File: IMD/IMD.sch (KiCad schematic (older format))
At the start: 6 parts

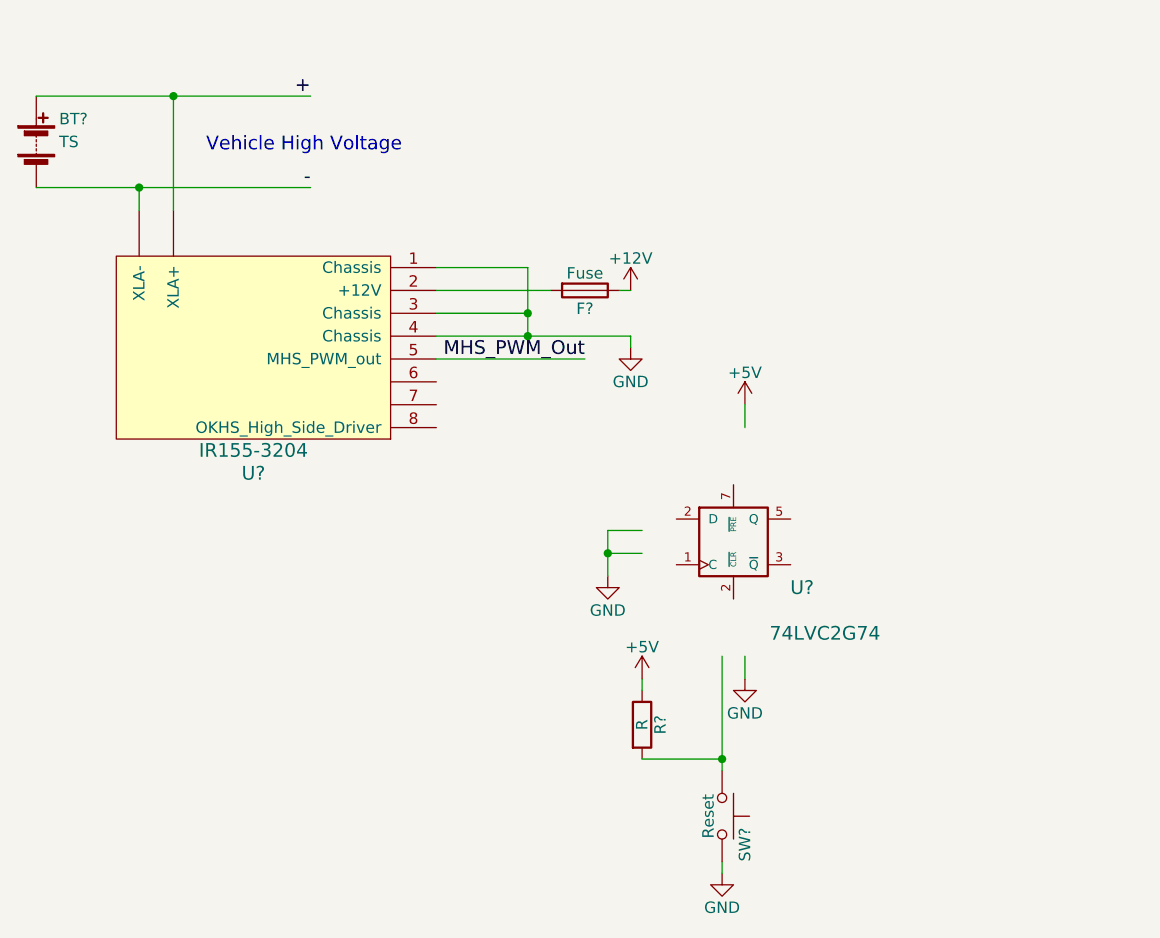
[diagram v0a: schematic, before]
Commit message: BSPD is more fleshed out. IMD latching continuing
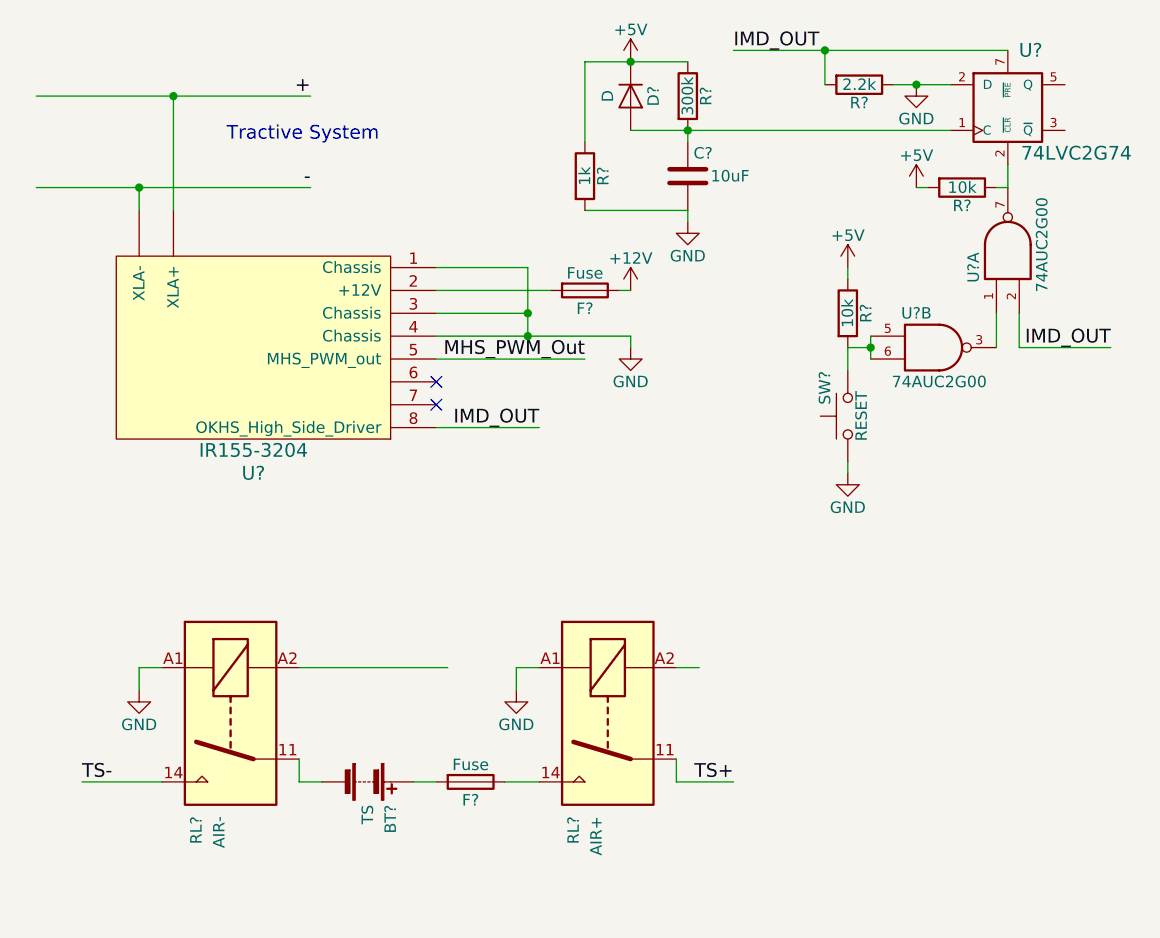
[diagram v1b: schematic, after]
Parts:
- removed R?: R, symbol R
- removed SW?: Reset, symbol SW_Push
- added C?: 10uF, symbol C
- added D?: D, symbol D
- added F?: Fuse, symbol Fuse
- added R?: 2.2k, symbol R
- added R?: 300k, symbol R
- added R?: 1k, symbol R
- added R? (x2): 10k, symbol R
- added RL?: AIR-, symbol Relay-SPST
- added RL?: AIR+, symbol Relay-SPST
- added SW?: RESET, symbol SW_Push
- added U? (x2): 74AUC2G00, symbol 74AUC2G00
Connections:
- net labels added: IMD_OUT, TS+, TS-
- wire segments 21 -> 46
- no-connect marks 0 -> 2
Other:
- note added: "Tractive System\n\n"
- note removed: "Vehicle High Voltage\n"
- moved on the sheet: BT?, U?

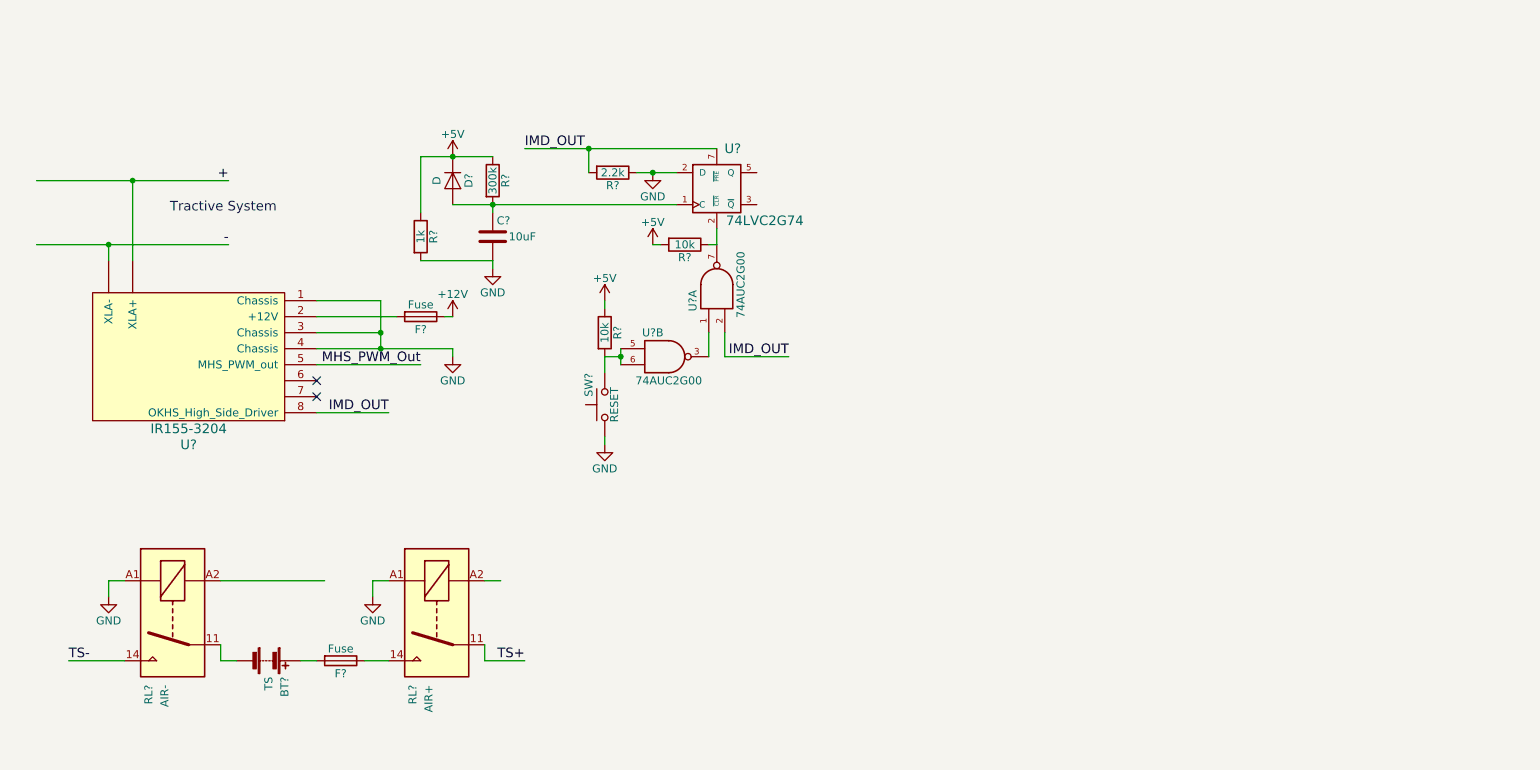
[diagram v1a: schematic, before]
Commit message: ESF-related changes to current system schematics
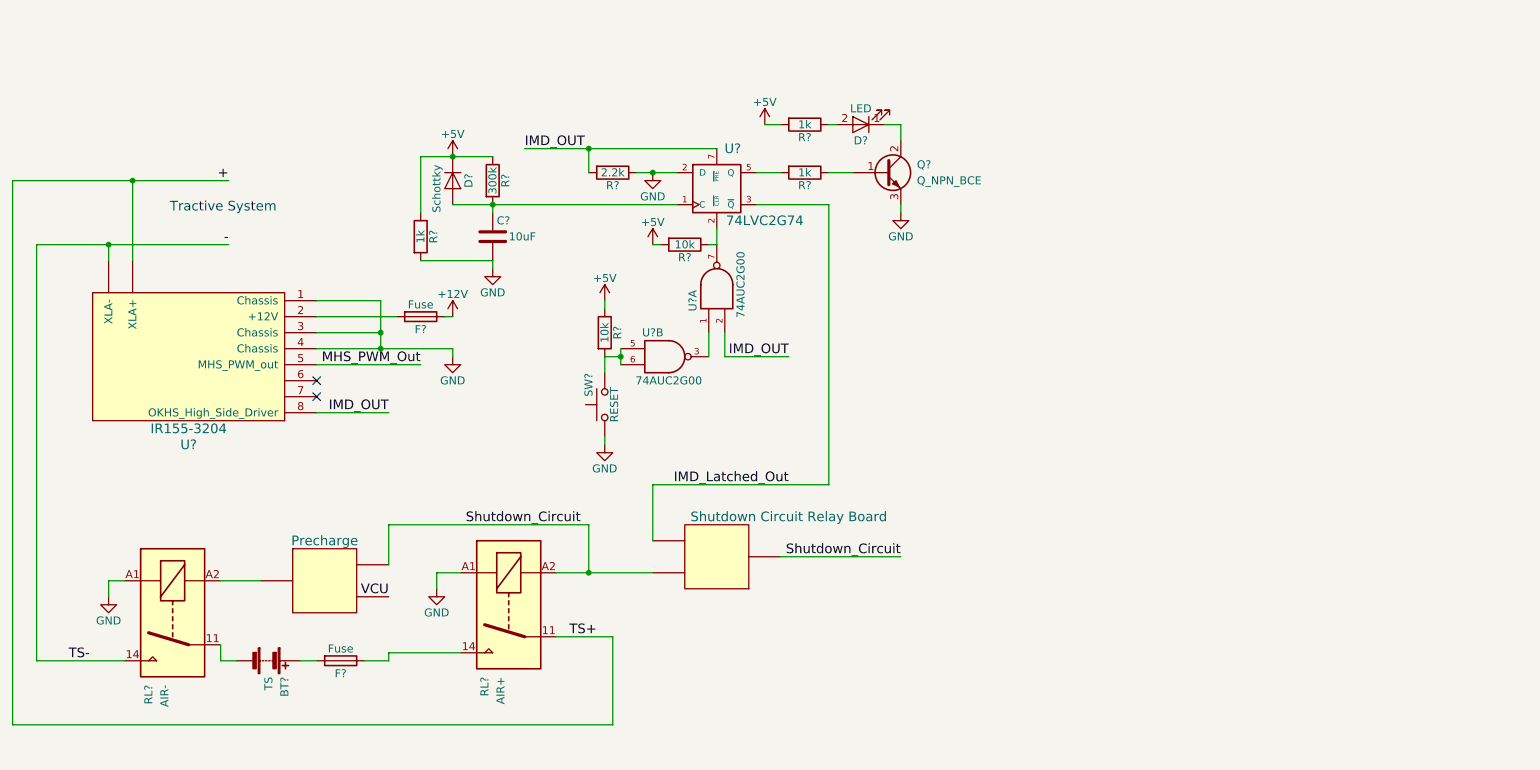
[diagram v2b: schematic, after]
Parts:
- added D?: LED, symbol LED
- added Q?: Q_NPN_BCE, symbol Q_NPN_BCE
- added R? (x2): 1k, symbol R
- added U?: Precharge, symbol Generic_1x2
- added U?: Shutdown Circuit Relay Board, symbol Generic_1x2
- D?: value D -> Schottky
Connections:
- net labels added: IMD_Latched_Out, Shutdown_Circuit, VCU
- wire segments 46 -> 66
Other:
- moved on the sheet: RL?
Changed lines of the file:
@@
 $EndComp
 Wire Wire Line
-	1600 1600 2800 1600
+	1450 1600 2800 1600
 Wire Wire Line
 	1600 2000 2800 2000
@@
 P 4200 1600
 F 0 "D?" H 4200 1700 50  0000 C CNN
-F 1 "D" H 4200 1500 50  0000 C CNN
+F 1 "Schottky" H 4250 1500 50  0000 C CNN
 F 2 "" H 4200 1600 50  0001 C CNN
 F 3 "" H 4200 1600 50  0001 C CNN
@@
 L Relay-SPST RL?
 U 1 1 58D08E57
-P 4100 4300
-F 0 "RL?" H 4550 4450 50  0000 L CNN
-F 1 "AIR+" H 4550 4350 50  0000 L CNN
-F 2 "" H 4100 4300 50  0000 C CNN
-F 3 "" H 4100 4300 50  0000 C CNN
-	1    4100 4300
+P 4550 4250
+F 0 "RL?" H 5000 4400 50  0000 L CNN
+F 1 "AIR+" H 5000 4300 50  0000 L CNN
+F 2 "" H 4550 4250 50  0000 C CNN
+F 3 "" H 4550 4250 50  0000 C CNN
+	1    4550 4250
 	0    -1   1    0
 $EndComp
@@
 Wire Wire Line
 	3650 4600 3800 4600
-Text Label 4650 4600 2    60   ~ 0
+Text Label 5100 4450 2    60   ~ 0
 TS+
-Wire Wire Line
-	4650 4600 4400 4600
 Text Label 1800 4600 0    60   ~ 0
 TS-
 Wire Wire Line
-	1800 4600 2150 4600
-Wire Wire Line
-	4400 4600 4400 4500
+	1600 4600 2150 4600
 Wire Wire Line
 	2750 4500 2750 4600
@@
 L GND #PWR?
 U 1 1 58D09A03
-P 3700 4200
-F 0 "#PWR?" H 3700 3950 50  0001 C CNN
-F 1 "GND" H 3700 4050 50  0000 C CNN
-F 2 "" H 3700 4200 50  0001 C CNN
-F 3 "" H 3700 4200 50  0001 C CNN
-	1    3700 4200
-	1    0    0    -1
-$EndComp
-Wire Wire Line
-	3700 4200 3700 4100
-Wire Wire Line
-	3700 4100 3800 4100
-Wire Wire Line
-	3400 4100 2750 4100
-Wire Wire Line
-	4500 4100 4400 4100
+P 4100 4150
+F 0 "#PWR?" H 4100 3900 50  0001 C CNN
+F 1 "GND" H 4100 4000 50  0000 C CNN
+F 2 "" H 4100 4150 50  0001 C CNN
+F 3 "" H 4100 4150 50  0001 C CNN
+	1    4100 4150
+	1    0    0    -1
+$EndComp
+Wire Wire Line
+	1600 4600 1600 2000
+Wire Wire Line
+	1450 5000 1450 1600
+$Comp
+L Generic_1x2 U?
+U 1 1 58D5B41B
+P 3400 4100
+F 0 "U?" H 3250 4350 60  0001 C CNN
+F 1 "Precharge" H 3400 4350 60  0000 C CNN
+F 2 "" H 3400 4100 60  0001 C CNN
+F 3 "" H 3400 4100 60  0001 C CNN
+	1    3400 4100
+	1    0    0    -1
+$EndComp
+Wire Wire Line
+	4100 4150 4100 4050
+Wire Wire Line
+	4100 4050 4250 4050
+Wire Wire Line
+	3800 4600 3800 4550
+Wire Wire Line
+	3800 4550 4250 4550
+Text Label 3800 4200 2    60   ~ 0
+VCU
+Wire Wire Line
+	3000 4100 2750 4100
+Wire Wire Line
+	3800 4000 3800 3750
+Wire Wire Line
+	3800 3750 5050 3750
+Wire Wire Line
+	5050 3750 5050 4050
+Wire Wire Line
+	4850 4050 5450 4050
+Wire Wire Line
+	4850 4450 5200 4450
+Wire Wire Line
+	5200 4450 5200 5000
+Wire Wire Line
+	5200 5000 1450 5000
+$Comp
+L Generic_1x2 U?
+U 1 1 58D5C58F
+P 5850 3950
+F 0 "U?" H 5700 4200 60  0001 C CNN
+F 1 "Shutdown Circuit Relay Board" H 5400 3700 60  0000 C CNN
+F 2 "" H 5850 3950 60  0001 C CNN
+F 3 "" H 5850 3950 60  0001 C CNN
+	1    5850 3950
+	-1   0    0    1
+$EndComp
+Connection ~ 5050 4050
+Text Label 7000 3950 2    60   ~ 0
+Shutdown_Circuit
+Wire Wire Line
+	7000 3950 6250 3950
+Text Label 5000 3750 2    60   ~ 0
+Shutdown_Circuit
+Wire Wire Line
+	6100 1750 6550 1750
+Wire Wire Line
+	6550 1750 6550 3500
+Wire Wire Line
+	6550 3500 5450 3500
+Wire Wire Line
+	5450 3500 5450 3850
+Text Label 6300 3500 2    60   ~ 0
+IMD_Latched_Out
+$Comp
+L Q_NPN_BCE Q?
+U 1 1 58D5D652
+P 6900 1550
+F 0 "Q?" H 7100 1600 50  0000 L CNN
+F 1 "Q_NPN_BCE" H 7100 1500 50  0000 L CNN
+F 2 "" H 7100 1650 50  0001 C CNN
+F 3 "" H 6900 1550 50  0001 C CNN
+	1    6900 1550
+	1    0    0    -1
+$EndComp
+$Comp
+L GND #PWR?
+U 1 1 58D5D69D
+P 7000 1800
+F 0 "#PWR?" H 7000 1550 50  0001 C CNN
+F 1 "GND" H 7000 1650 50  0000 C CNN
+F 2 "" H 7000 1800 50  0001 C CNN
+F 3 "" H 7000 1800 50  0001 C CNN
+	1    7000 1800
+	1    0    0    -1
+$EndComp
+Wire Wire Line
+	7000 1800 7000 1750
+$Comp
+L R R?
+U 1 1 58D5D7BE
+P 6400 1550
+F 0 "R?" V 6480 1550 50  0000 C CNN
+F 1 "1k" V 6400 1550 50  0000 C CNN
+F 2 "" V 6330 1550 50  0001 C CNN
+F 3 "" H 6400 1550 50  0001 C CNN
+	1    6400 1550
+	0    1    1    0
+$EndComp
+Wire Wire Line
+	6100 1550 6250 1550
+Wire Wire Line
+	6550 1550 6700 1550
+$Comp
+L LED D?
+U 1 1 58D5D93A
+P 6750 1250
+F 0 "D?" H 6750 1350 50  0000 C CNN
+F 1 "LED" H 6750 1150 50  0000 C CNN
+F 2 "" H 6750 1250 50  0001 C CNN
+F 3 "" H 6750 1250 50  0001 C CNN
+	1    6750 1250
+	-1   0    0    1
+$EndComp
+$Comp
+L R R?
+U 1 1 58D5D9A5
+P 6400 1250
+F 0 "R?" V 6480 1250 50  0000 C CNN
+F 1 "1k" V 6400 1250 50  0000 C CNN
+F 2 "" V 6330 1250 50  0001 C CNN
+F 3 "" H 6400 1250 50  0001 C CNN
+	1    6400 1250
+	0    1    1    0
+$EndComp
+$Comp
+L +5V #PWR?
+U 1 1 58D5D9F2
+P 6150 1250
+F 0 "#PWR?" H 6150 1100 50  0001 C CNN
+F 1 "+5V" H 6150 1390 50  0000 C CNN
+F 2 "" H 6150 1250 50  0001 C CNN
+F 3 "" H 6150 1250 50  0001 C CNN
+	1    6150 1250
+	1    0    0    -1
+$EndComp
+Wire Wire Line
+	6150 1250 6250 1250
+Wire Wire Line
+	6550 1250 6600 1250
+Wire Wire Line
+	6900 1250 7000 1250
+Wire Wire Line
+	7000 1250 7000 1350
 $EndSCHEMATC

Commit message: Tweaks to IMD and tsal for ESF
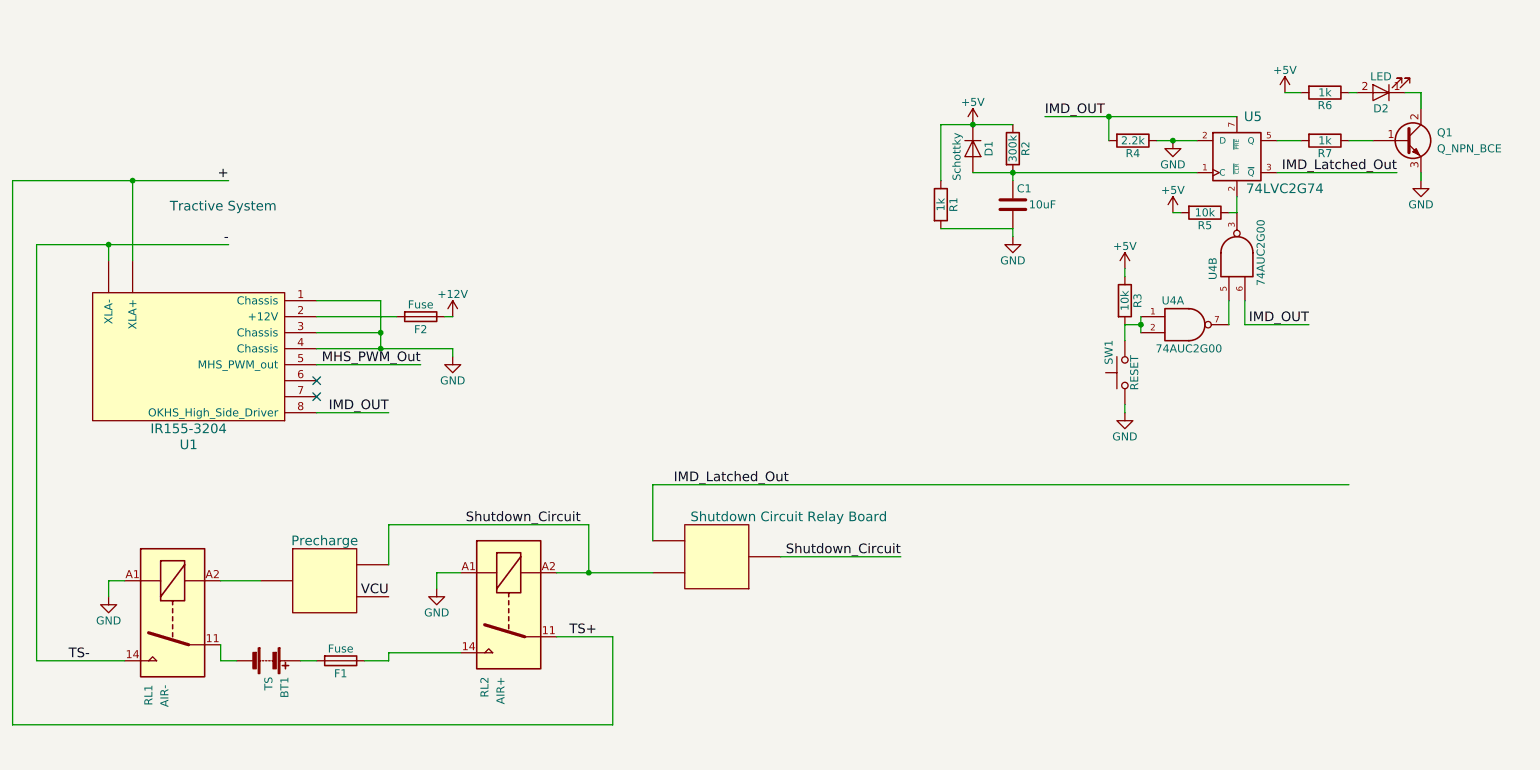
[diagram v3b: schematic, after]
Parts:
- gave numbers to parts that had none: 22
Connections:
- net IMD_OUT: now also U4.6; no longer U4.2
- net at R3.2, SW1.2: now also U4.1, U4.2; no longer U4.5, U4.6
- new net: R5.1, U4.3, U5.2 (~CLR)
- new net: U4.5, U4.7
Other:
- moved on the sheet: C1, D1, D2, Q1, R1, R2, R3, R4, R5, R6, R7, SW1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

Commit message: Decoupling caps annotated
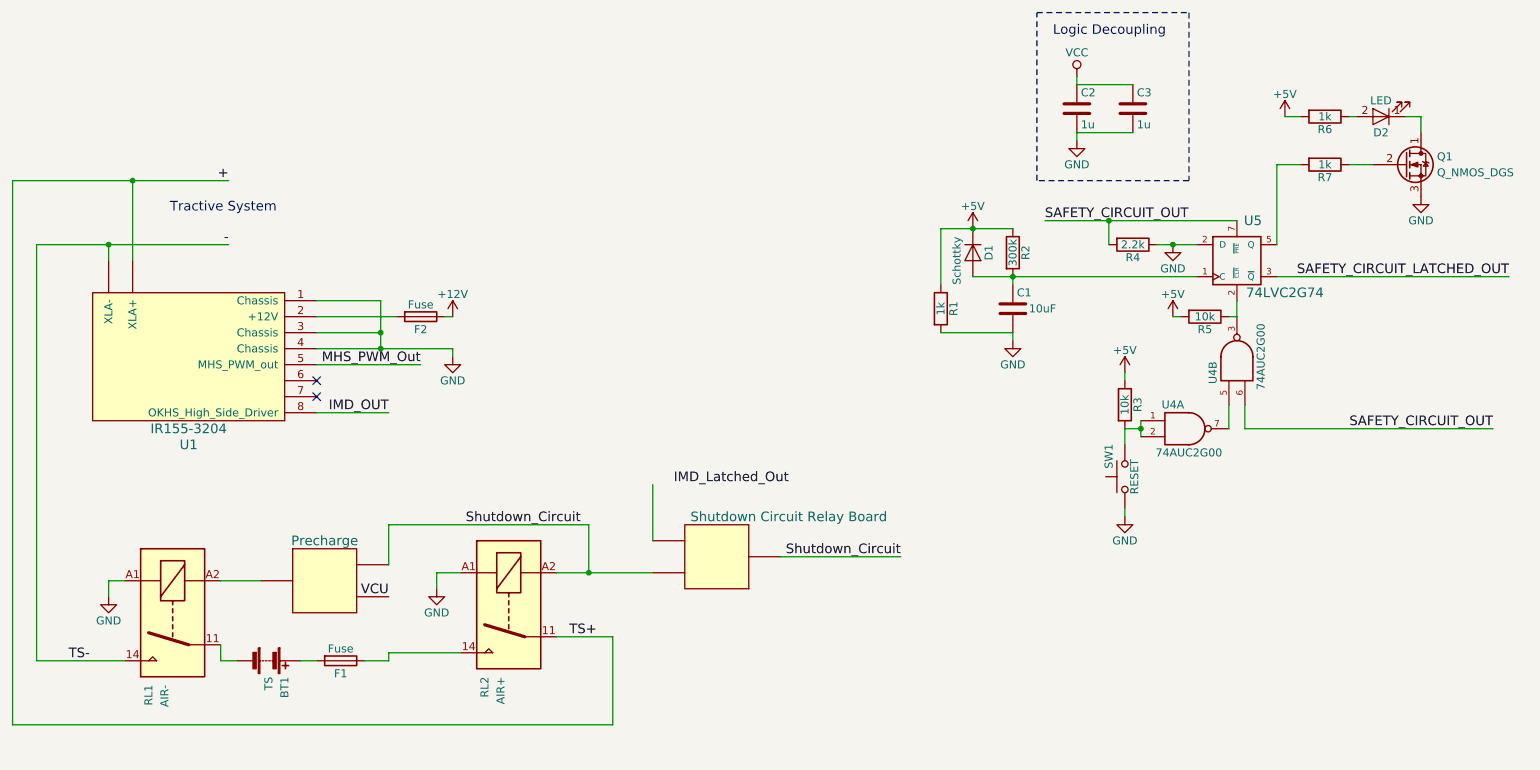
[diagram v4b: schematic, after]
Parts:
- removed Q1: Q_NPN_BCE, symbol Q_NPN_BCE
- added C2, C3: 1u, symbol C
- added Q1: Q_NMOS_DGS, symbol Q_NMOS_DGS
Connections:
- net GND: now also C2.2, C3.2, Q1.3 (S)
- net IMD_Latched_Out: no longer U3.~, U5.3 (~Q)
- net IMD_OUT: no longer R4.2, U4.6, U5.7 (~PRE)
- net VCC: now also C2.1, C3.1
- net at R7.1: now also Q1.2 (G)
- net at D2.1 (K): now also Q1.1 (D)
- new net SAFETY_CIRCUIT_LATCHED_OUT: U5.3 (~Q)
- new net SAFETY_CIRCUIT_OUT: R4.2, U4.6, U5.7 (~PRE)
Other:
- note added: "Logic Decoupling\n"
- moved on the sheet: C1, D1, D2, R1, R2, R3, R4, R5, R6, R7, SW1, U4A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

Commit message: Decoupling updates, small VCU changes
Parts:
- added C4, C5: 1u, symbol C
- added F3: Fuse, symbol Fuse
- added U6: LM1117-5.0, symbol LM1117-5.0
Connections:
- net labels removed: SAFETY_CIRCUIT_LATCHED_OUT, SAFETY_CIRCUIT_OUT
- wire segments 68 -> 74
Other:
- note added: "U4 Decoupling\nPlace close to pin 4\n"
- note added: "U5 Decoupling\nPlace close to pin 4\n"
- note removed: "Logic Decoupling\n"
- moved on the sheet: C1, C2, C3, D1, D2, Q1, R1, R2, R3, R4, R5, R6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
